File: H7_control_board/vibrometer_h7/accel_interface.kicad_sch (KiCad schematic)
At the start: 9 parts

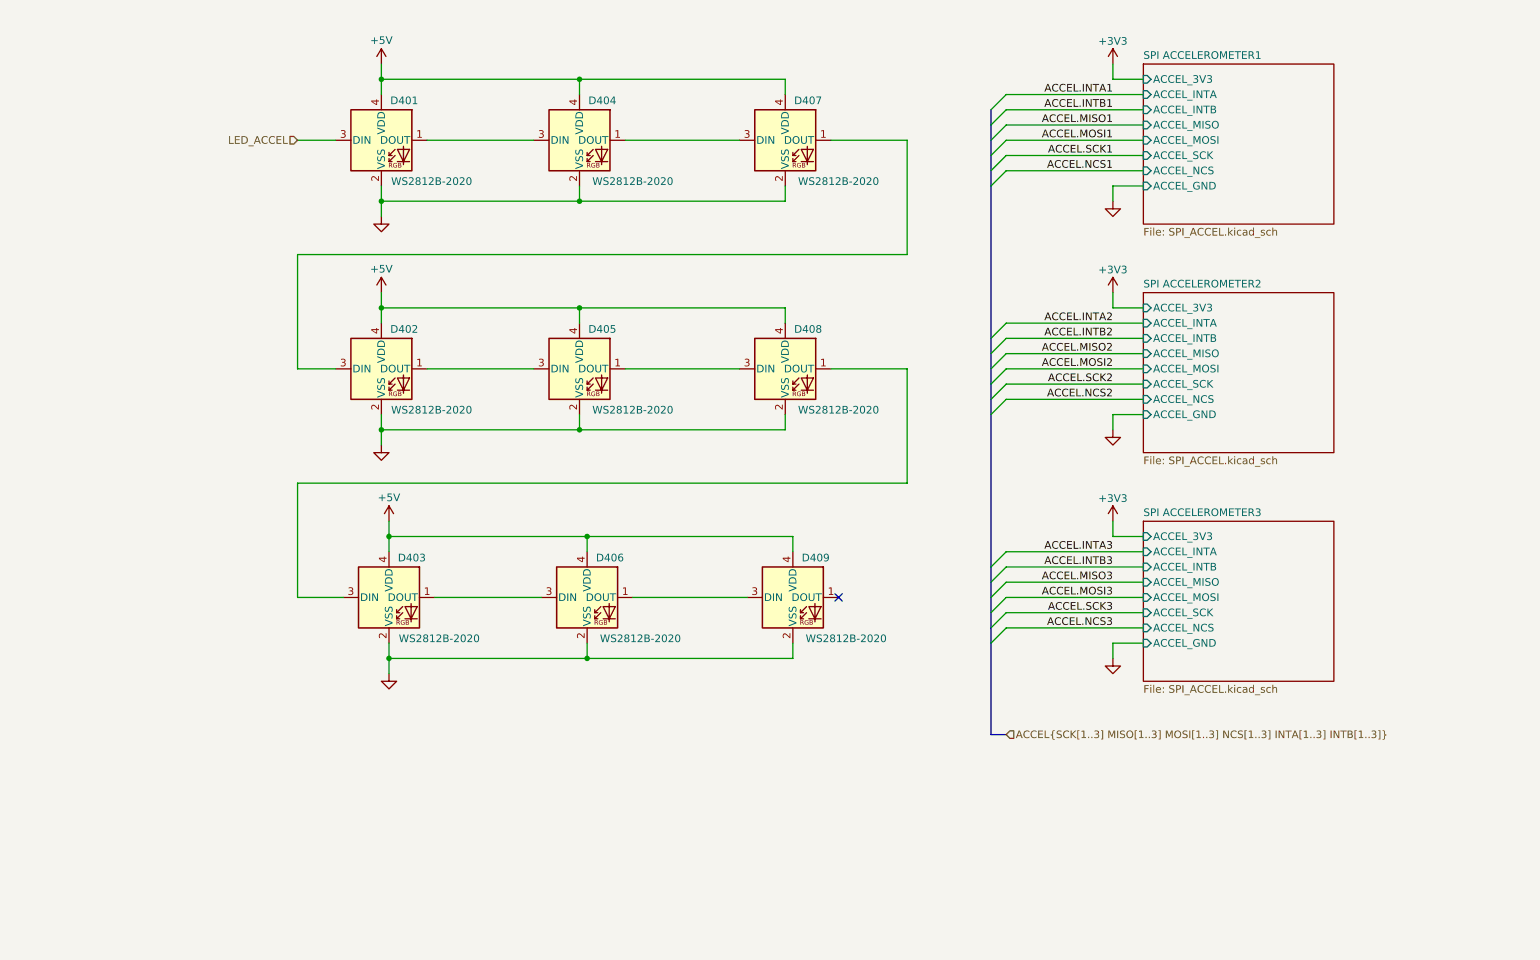
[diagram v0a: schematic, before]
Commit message: more decoupling caps, added level shifter to ws2812 led signal line
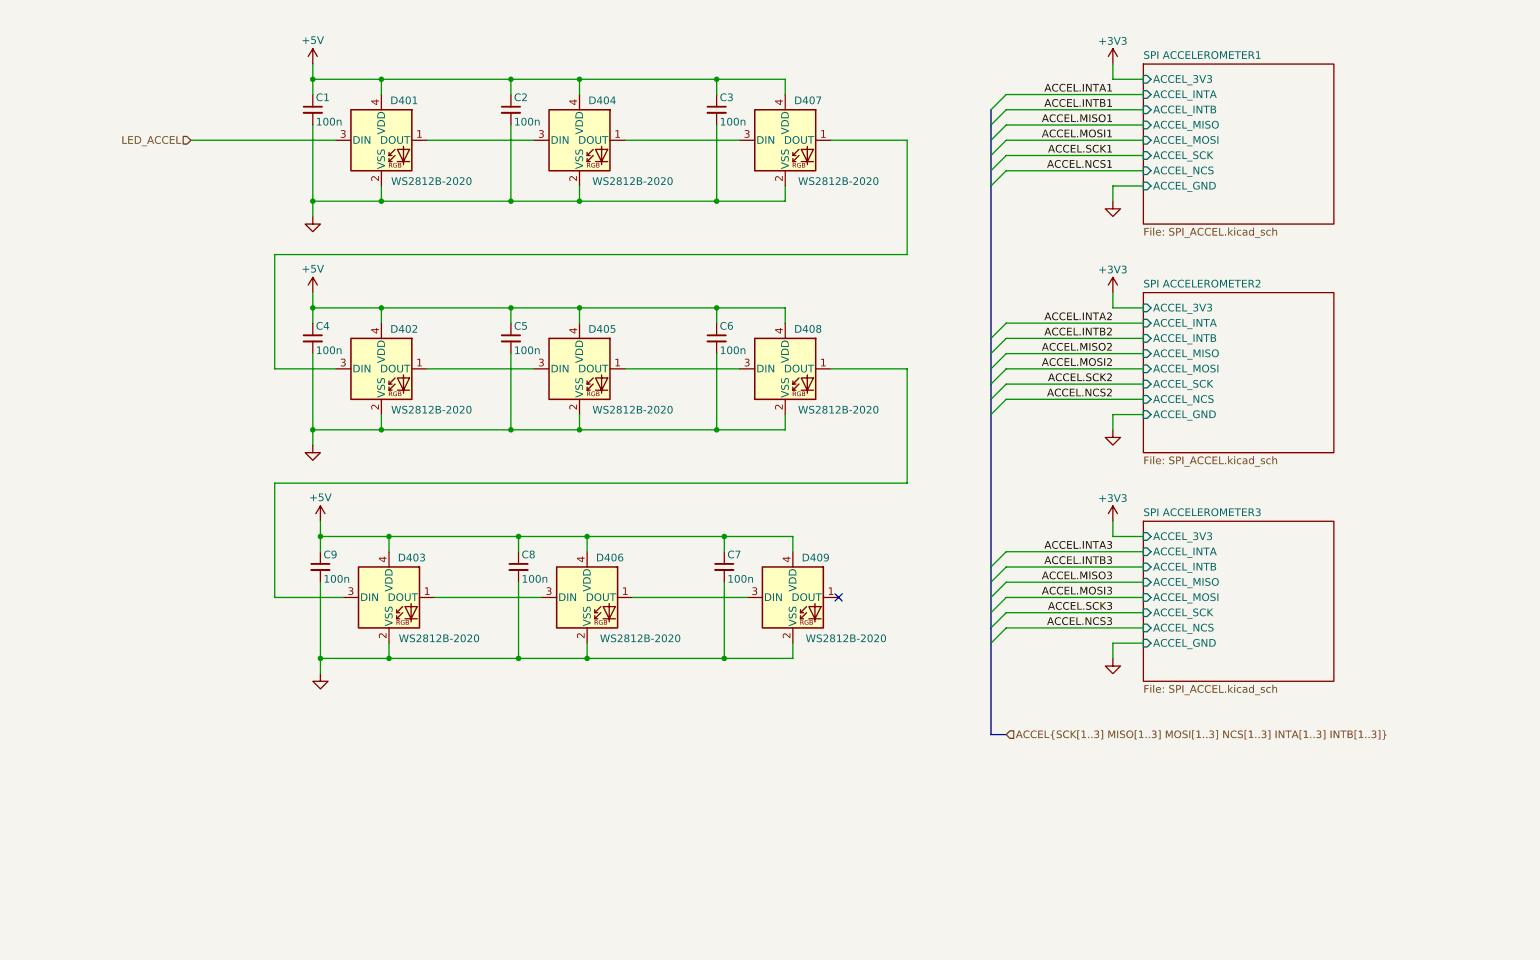
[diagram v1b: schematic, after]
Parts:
- added C1, C2, C3, C4, C5, C6, C7, C8, C9: 100n, symbol Device:C_Small
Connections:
- net +5V: now also C1.1, C2.1, C3.1, C4.1, C5.1, C6.1, C7.1, C8.1, C9.1
- net GND: now also C1.2, C2.2, C3.2, C4.2, C5.2, C6.2, C7.2, C8.2, C9.2

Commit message: selected strobe LEDs, schematic cleanup
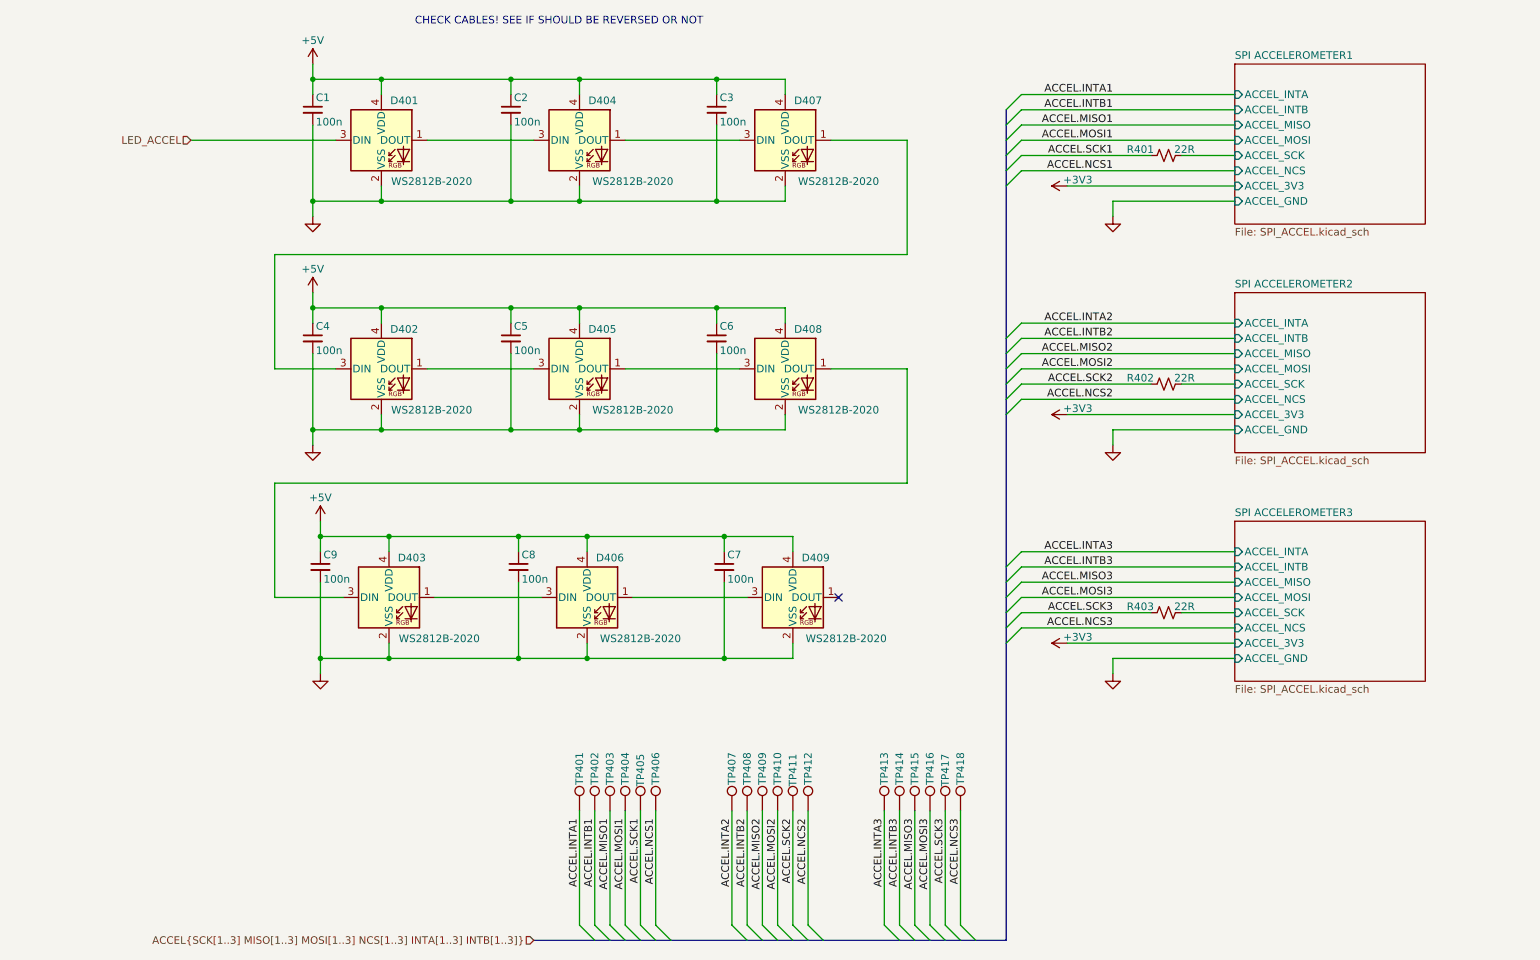
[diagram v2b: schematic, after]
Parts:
- added R401, R402, R403: 22R, symbol Device:R_Small_US
- added TP401, TP402, TP403, TP404, TP405, TP406, TP407, TP408, TP409, TP410, TP411, TP412, TP413, TP414, TP415, TP416, TP417, TP418: TestPoint, TestPoint:TestPoint_Pad_D1.5mm, symbol Connector:TestPoint
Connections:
- net ACCEL.INTA1: now also TP401.1
- net ACCEL.INTA2: now also TP407.1
- net ACCEL.INTA3: now also TP413.1
- net ACCEL.INTB1: now also TP402.1
- net ACCEL.INTB2: now also TP408.1
- net ACCEL.INTB3: now also TP414.1
- net ACCEL.MISO1: now also TP403.1
- net ACCEL.MISO2: now also TP409.1
- net ACCEL.MISO3: now also TP415.1
- net ACCEL.MOSI1: now also TP404.1
- net ACCEL.MOSI2: now also TP410.1
- net ACCEL.MOSI3: now also TP416.1
- net ACCEL.NCS1: now also TP406.1
- net ACCEL.NCS2: now also TP412.1
- net ACCEL.NCS3: now also TP418.1
- net ACCEL.SCK1: now also R401.2, TP405.1
- net ACCEL.SCK2: now also R402.2, TP411.1
- net ACCEL.SCK3: now also R403.2, TP417.1
- new net SPI ACCELEROMETER1/ACCEL_SCK: R401.1
- new net SPI ACCELEROMETER2/ACCEL_SCK: R402.1
- new net SPI ACCELEROMETER3/ACCEL_SCK: R403.1
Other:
- note added: "CHECK CABLES! SEE IF SHOULD BE REVERSED OR NOT"

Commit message: first pass at board routing
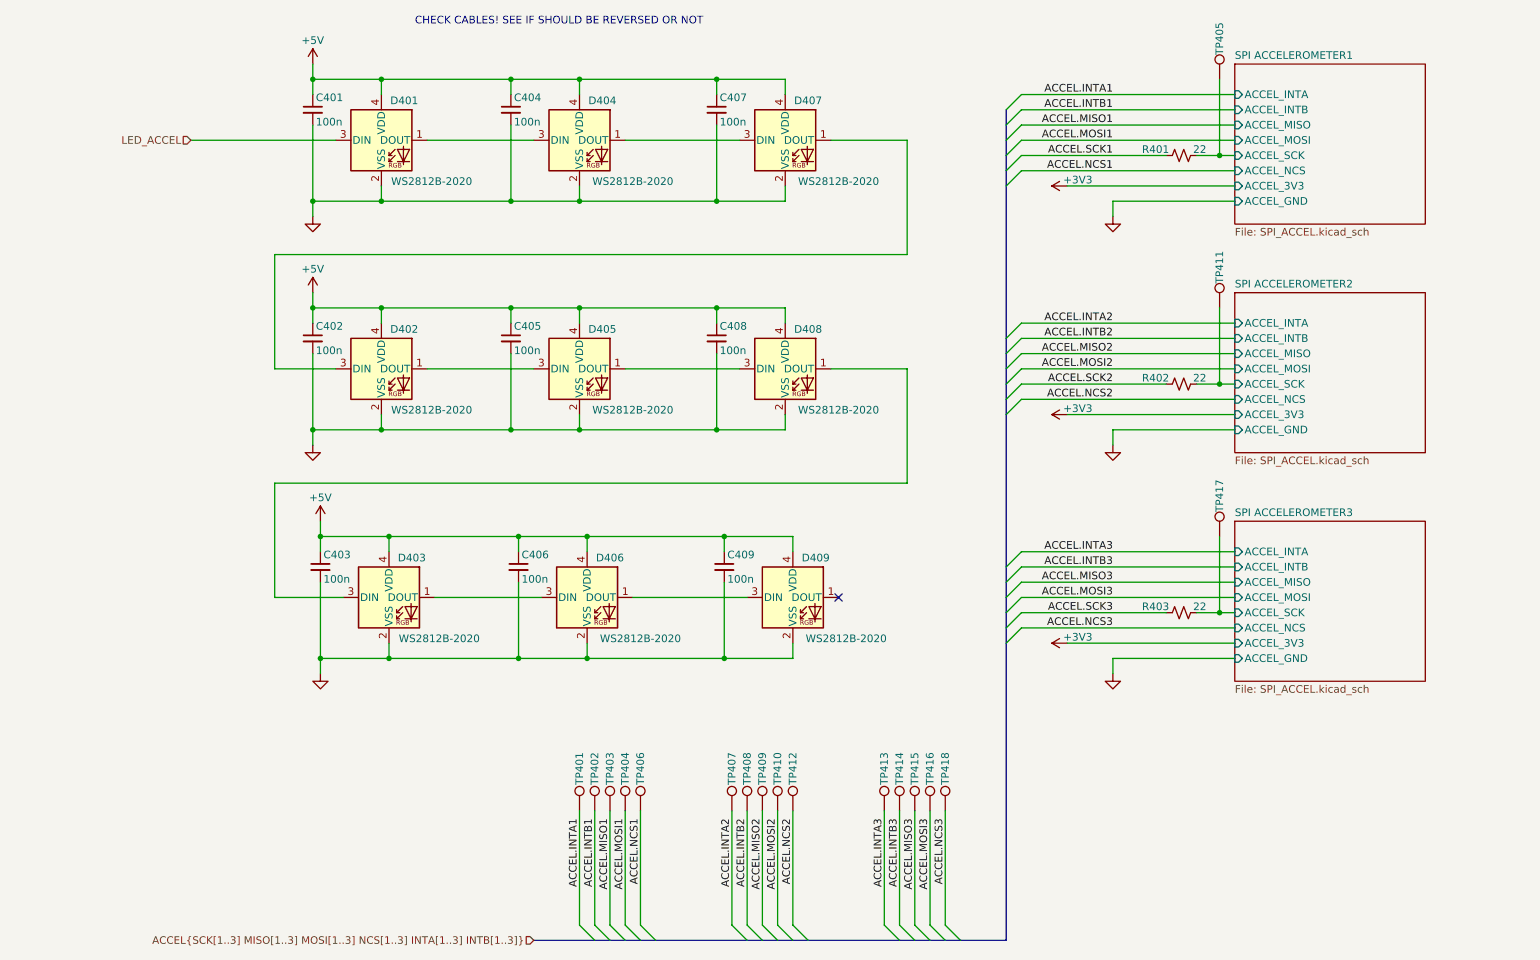
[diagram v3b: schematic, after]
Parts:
- C401: renamed from C1; footprint (none) -> Capacitor_SMD:C_0402_1005Metric_Pad0.74x0.62mm_HandSolder; LCSC (none) -> C307331
- C402: renamed from C4; footprint (none) -> Capacitor_SMD:C_0402_1005Metric_Pad0.74x0.62mm_HandSolder; LCSC (none) -> C307331
- C403: renamed from C9; footprint (none) -> Capacitor_SMD:C_0402_1005Metric_Pad0.74x0.62mm_HandSolder; LCSC (none) -> C307331
- C404: renamed from C2; footprint (none) -> Capacitor_SMD:C_0402_1005Metric_Pad0.74x0.62mm_HandSolder; LCSC (none) -> C307331
- C405: renamed from C5; footprint (none) -> Capacitor_SMD:C_0402_1005Metric_Pad0.74x0.62mm_HandSolder; LCSC (none) -> C307331
- C406: renamed from C8; footprint (none) -> Capacitor_SMD:C_0402_1005Metric_Pad0.74x0.62mm_HandSolder; LCSC (none) -> C307331
- C407: renamed from C3; footprint (none) -> Capacitor_SMD:C_0402_1005Metric_Pad0.74x0.62mm_HandSolder; LCSC (none) -> C307331
- C408: renamed from C6; footprint (none) -> Capacitor_SMD:C_0402_1005Metric_Pad0.74x0.62mm_HandSolder; LCSC (none) -> C307331
- C409: renamed from C7; footprint (none) -> Capacitor_SMD:C_0402_1005Metric_Pad0.74x0.62mm_HandSolder; LCSC (none) -> C307331
- R401, R402, R403: value 22R -> 22; footprint (none) -> Resistor_SMD:R_0402_1005Metric; LCSC (none) -> C25092
- TP401, TP402, TP403, TP404, TP405, TP406, TP407, TP408, TP409, TP410, TP411, TP412, TP413, TP414, TP415, TP416, TP417, TP418: footprint TestPoint:TestPoint_Pad_D1.5mm -> TestPoint:TestPoint_Pad_D1.0mm
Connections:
- net ACCEL.SCK1: no longer TP405.1
- net ACCEL.SCK2: no longer TP411.1
- net ACCEL.SCK3: no longer TP417.1
- net SPI ACCELEROMETER1/ACCEL_SCK: now also TP405.1
- net SPI ACCELEROMETER2/ACCEL_SCK: now also TP411.1
- net SPI ACCELEROMETER3/ACCEL_SCK: now also TP417.1
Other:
- moved on the sheet: R401, R402, R403, TP406, TP412, TP417, TP418

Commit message: lots of routing progress!!
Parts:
- renumbered C404 to C402, C407 to C403, C402 to C404, C408 to C406, C403 to C407, C406 to C408, D404 to D402, D407 to D403, D402 to D404, D408 to D406, D403 to D407, D406 to D408, TP405 to TP401, TP411 to TP402, TP417 to TP403, TP401 to TP404, TP402 to TP405, TP403 to TP406, TP404 to TP407, TP406 to TP408, TP407 to TP409, TP408 to TP410, TP409 to TP411, TP410 to TP412, TP412 to TP413, TP413 to TP414, TP414 to TP415, TP415 to TP416, TP416 to TP417

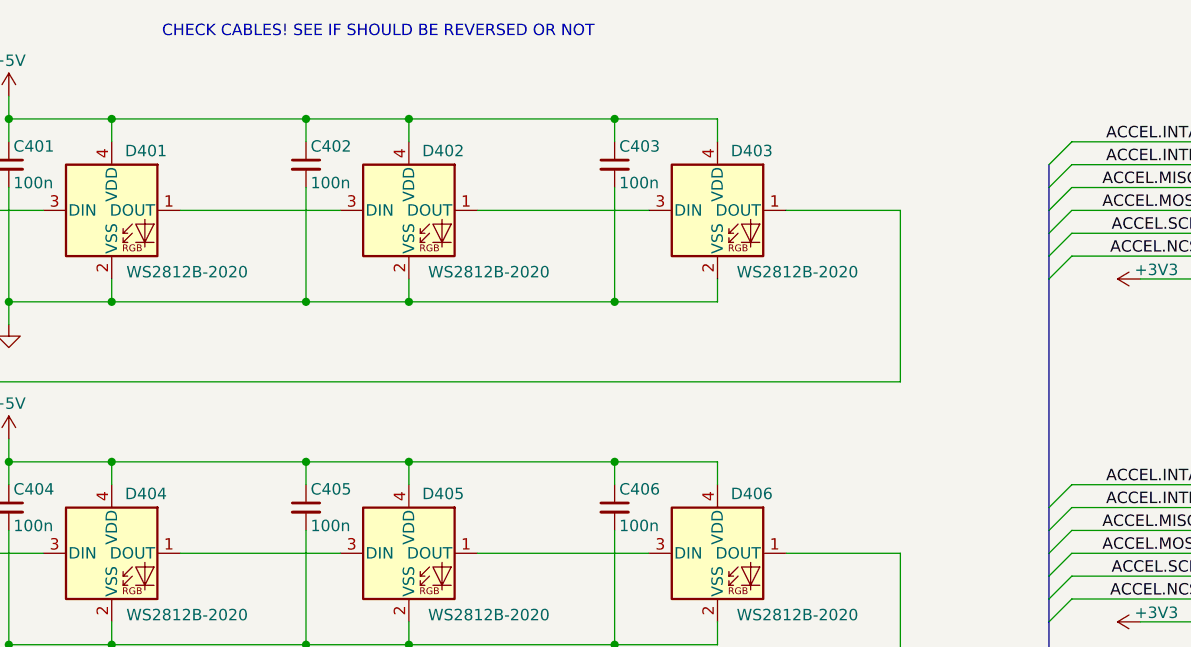
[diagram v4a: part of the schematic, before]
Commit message: added indicator leds
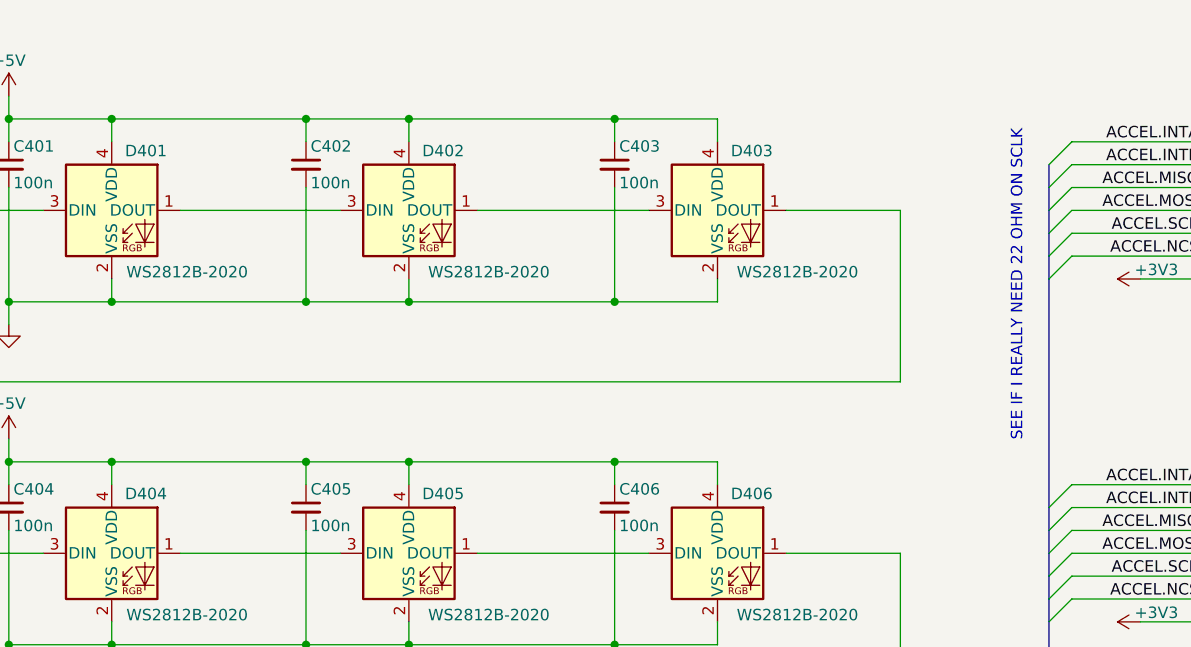
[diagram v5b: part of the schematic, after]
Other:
- note added: "SEE IF I REALLY NEED 22 OHM ON SCLK"
- note removed: "CHECK CABLES! SEE IF SHOULD BE REVERSED OR NOT"
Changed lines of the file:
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@@
 		)
 	)
-	(text "CHECK CABLES! SEE IF SHOULD BE REVERSED OR NOT"
+	(text "SEE IF I REALLY NEED 22 OHM ON SCLK"
 		(exclude_from_sim no)
-		(at 69.088 30.988 0)
+		(at 164.084 59.182 90)
 		(effects
 			(font
 				(size 1.27 1.27)
 			)
-			(justify left)
 		)
 	)

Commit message: nearly done....
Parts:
- C401, C402, C403, C404, C405, C406, C407, C408, C409: footprint Capacitor_SMD:C_0402_1005Metric_Pad0.74x0.62mm_HandSolder -> Capacitor_SMD:C_0402_1005Metric
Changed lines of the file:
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@@
 			)
 		)
-		(property "Footprint" "Capacitor_SMD:C_0402_1005Metric_Pad0.74x0.62mm_HandSolder"
+		(property "Footprint" "Capacitor_SMD:C_0402_1005Metric"
 			(at 85.09 83.82 0)
 			(effects
@@
 			)
 		)
-		(property "Footprint" "Capacitor_SMD:C_0402_1005Metric_Pad0.74x0.62mm_HandSolder"
+		(property "Footprint" "Capacitor_SMD:C_0402_1005Metric"
 			(at 52.07 45.72 0)
 			(effects
@@
 			)
 		)
-		(property "Footprint" "Capacitor_SMD:C_0402_1005Metric_Pad0.74x0.62mm_HandSolder"
+		(property "Footprint" "Capacitor_SMD:C_0402_1005Metric"
 			(at 52.07 83.82 0)
 			(effects
@@
 			)
 		)
-		(property "Footprint" "Capacitor_SMD:C_0402_1005Metric_Pad0.74x0.62mm_HandSolder"
+		(property "Footprint" "Capacitor_SMD:C_0402_1005Metric"
 			(at 119.38 83.82 0)
 			(effects
@@
 			)
 		)
-		(property "Footprint" "Capacitor_SMD:C_0402_1005Metric_Pad0.74x0.62mm_HandSolder"
+		(property "Footprint" "Capacitor_SMD:C_0402_1005Metric"
 			(at 119.38 45.72 0)
 			(effects
@@
 			)
 		)
-		(property "Footprint" "Capacitor_SMD:C_0402_1005Metric_Pad0.74x0.62mm_HandSolder"
+		(property "Footprint" "Capacitor_SMD:C_0402_1005Metric"
 			(at 53.34 121.92 0)
 			(effects
@@
 			)
 		)
-		(property "Footprint" "Capacitor_SMD:C_0402_1005Metric_Pad0.74x0.62mm_HandSolder"
+		(property "Footprint" "Capacitor_SMD:C_0402_1005Metric"
 			(at 85.09 45.72 0)
 			(effects
@@
 			)
 		)
-		(property "Footprint" "Capacitor_SMD:C_0402_1005Metric_Pad0.74x0.62mm_HandSolder"
+		(property "Footprint" "Capacitor_SMD:C_0402_1005Metric"
 			(at 120.65 121.92 0)
 			(effects
@@
 			)
 		)
-		(property "Footprint" "Capacitor_SMD:C_0402_1005Metric_Pad0.74x0.62mm_HandSolder"
+		(property "Footprint" "Capacitor_SMD:C_0402_1005Metric"
 			(at 86.36 121.92 0)
 			(effects

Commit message: checked all footprints, made tiny daughterboard
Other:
- note removed: "SEE IF I REALLY NEED 22 OHM ON SCLK"
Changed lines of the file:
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@@
-		)
-	)
-	(text "SEE IF I REALLY NEED 22 OHM ON SCLK"
-		(exclude_from_sim no)
-		(at 164.084 59.182 90)
-		(effects
-			(font
-				(size 1.27 1.27)
-			)
 		)
 	)
